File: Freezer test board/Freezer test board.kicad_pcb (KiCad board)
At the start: 4 copper layers, 56 x 65 mm, 24 parts, among them J2 Conn_02x20_Odd_Even, J3 284391-3, J4 284391-3, J5 284391-3, J6 284391-3, J7 284391-3, J8 284391-3, J9 284391-3

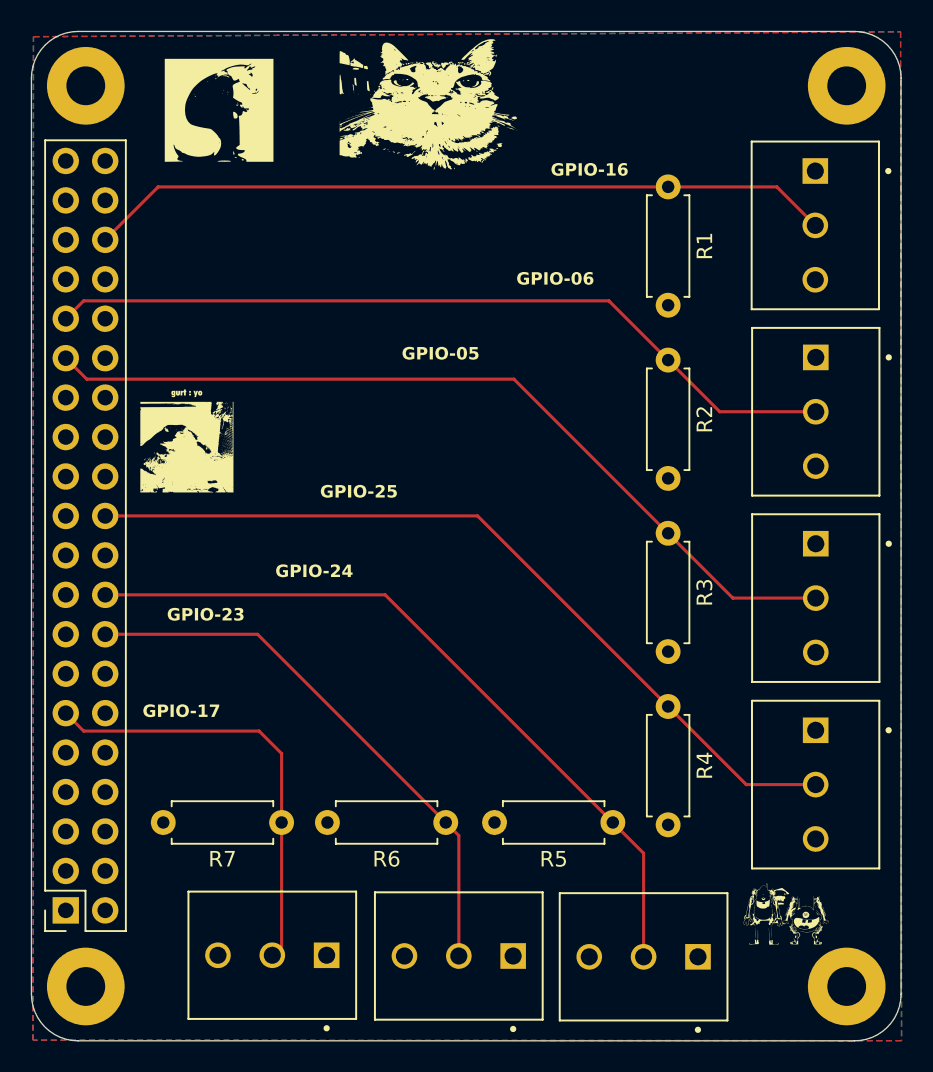
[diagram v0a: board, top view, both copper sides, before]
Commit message: Filled copper, adjust mask+silkscreens arts
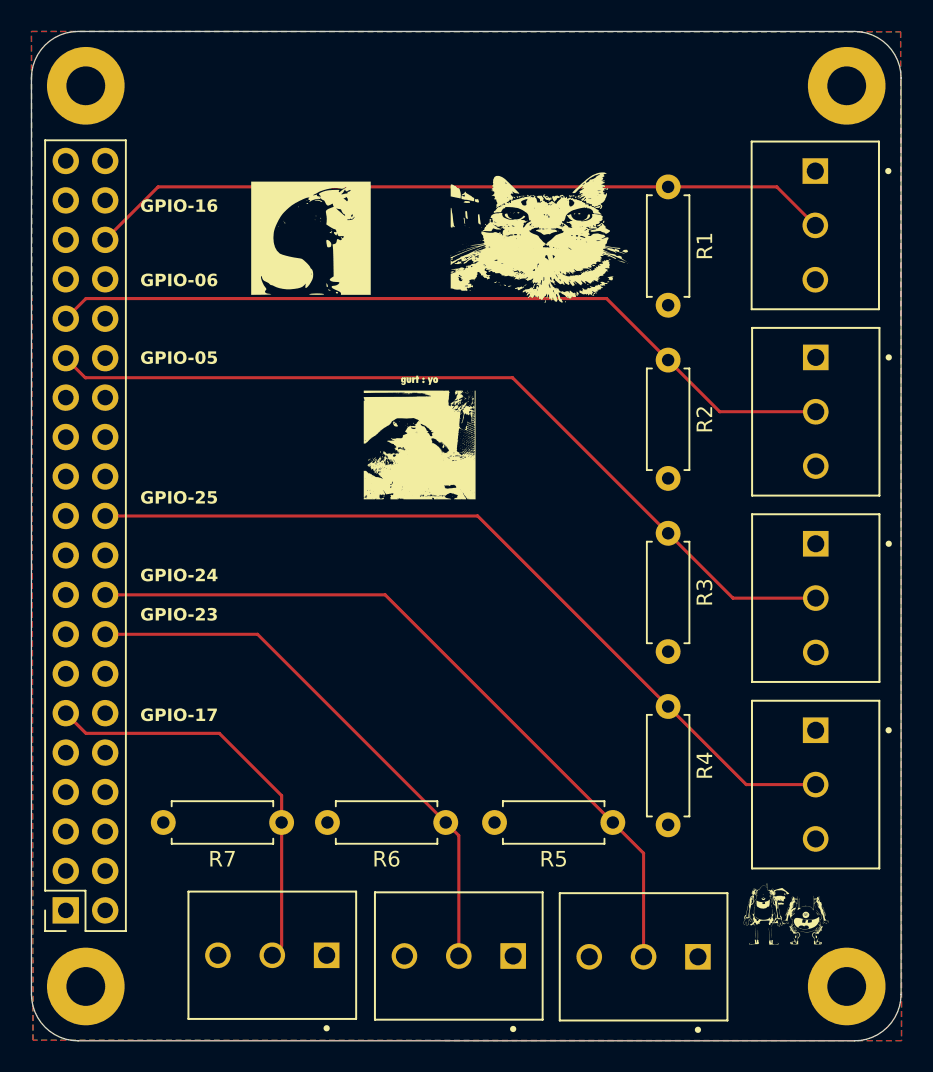
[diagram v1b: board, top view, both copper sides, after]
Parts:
- moved G*** 15.0 mm to (110.5, 63.0)
- moved G*** 11.2 mm to (118.5, 50.0)
- moved G*** 10.1 mm to (104.5, 50.0)
- moved G*** 4.01 mm to (111.5, 69.5)
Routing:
- net GPIO17: track 28.2 -> 26.6 mm
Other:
- board text added: "67 reviews later..."
- board text added: "Bronco STAR BLADE '26"
- board text added: "Designed by Jason Suarez"
- board text added: "Freezer Test Pi HAT 1.0"
- board text removed: "Freezer Test PCB"
- board text removed: "Made By Jason Suarez"

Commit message: Adjust mounting hole footprint to 2.7mm M2.5
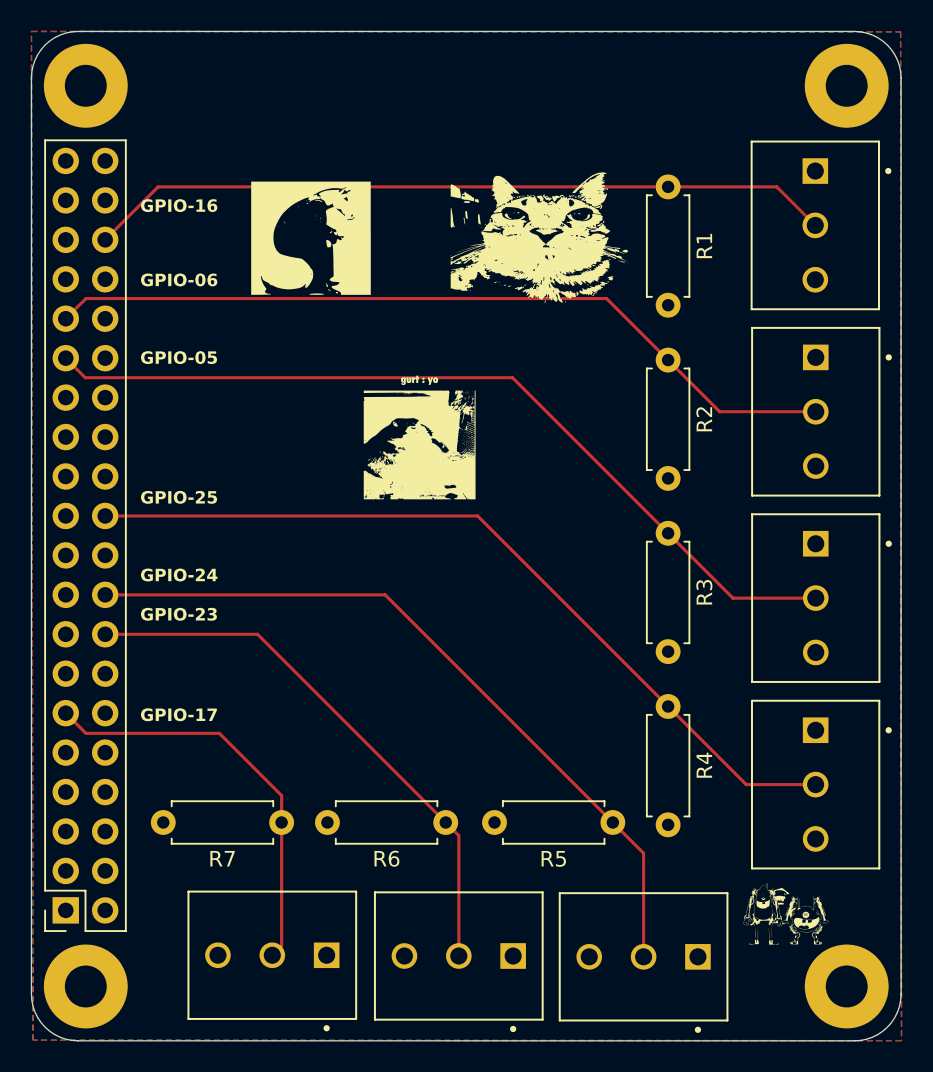
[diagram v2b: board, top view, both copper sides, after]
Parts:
- H1, H2, H3, H4: footprint MountingHole:MountingHole_2.5mm_Pad -> MountingHole:MountingHole_2.7mm_M2.5_Pad
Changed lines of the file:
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@@
 			)
 		)
-		(property "Datasheet" "~"
+		(property "Datasheet" ""
 			(at 0 0 180)
 			(layer "F.Fab")
@@
 			)
 		)
-		(property "Datasheet" "~"
+		(property "Datasheet" ""
 			(at 0 0 90)
 			(layer "F.Fab")
@@
 			)
 		)
-		(property "Datasheet" "~"
+		(property "Datasheet" ""
 			(at 0 0 0)
 			(layer "F.Fab")
@@
 			)
 		)
-		(property "Datasheet" "~"
+		(property "Datasheet" ""
 			(at 0 0 270)
 			(layer "F.Fab")
@@
 		)
 	)
-	(footprint "MountingHole:MountingHole_2.5mm_Pad"
+	(footprint "MountingHole:MountingHole_2.7mm_M2.5_Pad"
 		(layer "F.Cu")
 		(at 89 98.5)
-		(descr "Mounting Hole 2.5mm, generated by kicad-footprint-generator mountinghole.py")
-		(tags "mountinghole")
+		(descr "Mounting Hole 2.7mm, M2.5, generated by kicad-footprint-generator mountinghole.py")
+		(tags "mountinghole M2.5")
 		(property "Reference" "H2"
-			(at 4.61 0 0)
+			(at 0 -3.65 0)
 			(layer "F.SilkS")
 			(hide yes)
@@
 		)
 		(property "Value" "MountingHole"
-			(at 0 3.45 0)
+			(at 0 3.65 0)
 			(layer "F.Fab")
 			(effects
@@
 			)
 		)
-		(property "Datasheet" "~"
+		(property "Datasheet" ""
 			(at 0 0 0)
 			(layer "F.Fab")
@@
 		(sheetname "/")
 		(sheetfile "Freezer test board.kicad_sch")
-		(attr through_hole exclude_from_pos_files exclude_from_bom)
+		(attr exclude_from_pos_files exclude_from_bom)
 		(fp_circle
 			(center 0 0)
-			(end 2.5 0)
+			(end 2.7 0)
 			(stroke
 				(width 0.15)
@@
 		(fp_circle
 			(center 0 0)
-			(end 2.75 0)
+			(end 2.95 0)
 			(stroke
 				(width 0.05)
@@
 		(pad "1" thru_hole circle
 			(at 0 0)
-			(size 5 5)
-			(drill 2.5)
+			(size 5.4 5.4)
+			(drill 2.7)
 			(layers "*.Cu" "*.Mask")
 			(remove_unused_layers no)
@@
 			)
 		)
-		(property "Datasheet" "~"
+		(property "Datasheet" ""
 			(at 0 0 270)
 			(layer "F.Fab")
@@
 		)
 	)
-	(footprint "MountingHole:MountingHole_2.5mm_Pad"
+	(footprint "MountingHole:MountingHole_2.7mm_M2.5_Pad"
 		(layer "F.Cu")
 		(at 138 98.5)
-		(descr "Mounting Hole 2.5mm, generated by kicad-footprint-generator mountinghole.py")
-		(tags "mountinghole")
+		(descr "Mounting Hole 2.7mm, M2.5, generated by kicad-footprint-generator mountinghole.py")
+		(tags "mountinghole M2.5")
 		(property "Reference" "H4"
-			(at -4.23 -0.02 0)
+			(at 0 -3.65 0)
 			(layer "F.SilkS")
 			(hide yes)
@@
 		)
 		(property "Value" "MountingHole"
-			(at 0 3.45 0)
+			(at 0 3.65 0)
 			(layer "F.Fab")
 			(effects
@@
 			)
 		)
-		(property "Datasheet" "~"
+		(property "Datasheet" ""
 			(at 0 0 0)
 			(layer "F.Fab")
@@
 		(sheetname "/")
 		(sheetfile "Freezer test board.kicad_sch")
-		(attr through_hole exclude_from_pos_files exclude_from_bom)
+		(attr exclude_from_pos_files exclude_from_bom)
 		(fp_circle
 			(center 0 0)
-			(end 2.5 0)
+			(end 2.7 0)
 			(stroke
 				(width 0.15)
@@
 		(fp_circle
 			(center 0 0)
-			(end 2.75 0)
+			(end 2.95 0)
 			(stroke
 				(width 0.05)
@@
 		(pad "1" thru_hole circle
 			(at 0 0)
-			(size 5 5)
-			(drill 2.5)
+			(size 5.4 5.4)
+			(drill 2.7)
 			(layers "*.Cu" "*.Mask")
 			(remove_unused_layers no)
@@
 			)
 		)
-		(property "Datasheet" "~"
+		(property "Datasheet" ""
 			(at 0 0 270)
 			(layer "F.Fab")
@@
 			)
 		)
-		(property "Datasheet" "~"
+		(property "Datasheet" ""
 			(at 0 0 180)
 			(layer "F.Fab")
@@
 		)
 	)
-	(footprint "MountingHole:MountingHole_2.5mm_Pad"
+	(footprint "MountingHole:MountingHole_2.7mm_M2.5_Pad"
 		(layer "F.Cu")
 		(at 138 40.5)
-		(descr "Mounting Hole 2.5mm, generated by kicad-footprint-generator mountinghole.py")
-		(tags "mountinghole")
+		(descr "Mounting Hole 2.7mm, M2.5, generated by kicad-footprint-generator mountinghole.py")
+		(tags "mountinghole M2.5")
 		(property "Reference" "H3"
-			(at -4.48 0.05 0)
+			(at 0 -3.65 0)
 			(layer "F.SilkS")
 			(hide yes)
@@
 		)
 		(property "Value" "MountingHole"
-			(at 0 3.45 0)
+			(at 0 3.65 0)
 			(layer "F.Fab")
 			(effects
@@
 			)
 		)
-		(property "Datasheet" "~"
+		(property "Datasheet" ""
 			(at 0 0 0)
 			(layer "F.Fab")
@@
 		(sheetname "/")
 		(sheetfile "Freezer test board.kicad_sch")
-		(attr through_hole exclude_from_pos_files exclude_from_bom)
+		(attr exclude_from_pos_files exclude_from_bom)
 		(fp_circle
 			(center 0 0)
-			(end 2.5 0)
+			(end 2.7 0)
 			(stroke
 				(width 0.15)
@@
 		(fp_circle
 			(center 0 0)
-			(end 2.75 0)
+			(end 2.95 0)
 			(stroke
 				(width 0.05)
@@
 		(pad "1" thru_hole circle
 			(at 0 0)
-			(size 5 5)
-			(drill 2.5)
+			(size 5.4 5.4)
+			(drill 2.7)
 			(layers "*.Cu" "*.Mask")
 			(remove_unused_layers no)
@@
 			)
 		)
-		(property "Datasheet" "~"
+		(property "Datasheet" ""
 			(at 0 0 180)
 			(layer "F.Fab")
@@
 		(embedded_fonts no)
 	)
-	(footprint "MountingHole:MountingHole_2.5mm_Pad"
+	(footprint "MountingHole:MountingHole_2.7mm_M2.5_Pad"
 		(layer "F.Cu")
 		(at 89 40.5)
-		(descr "Mounting Hole 2.5mm, generated by kicad-footprint-generator mountinghole.py")
-		(tags "mountinghole")
+		(descr "Mounting Hole 2.7mm, M2.5, generated by kicad-footprint-generator mountinghole.py")
+		(tags "mountinghole M2.5")
 		(property "Reference" "H1"
-			(at 3.92 0.02 0)
+			(at 0 -3.65 0)
 			(layer "F.SilkS")
 			(hide yes)
@@
 		)
 		(property "Value" "MountingHole"
-			(at 0 3.45 0)
+			(at 0 3.65 0)
 			(layer "F.Fab")
 			(effects
@@
 			)
 		)
-		(property "Datasheet" "~"
+		(property "Datasheet" ""
 			(at 0 0 0)
 			(layer "F.Fab")
@@
 		(sheetname "/")
 		(sheetfile "Freezer test board.kicad_sch")
-		(attr through_hole exclude_from_pos_files exclude_from_bom)
+		(attr exclude_from_pos_files exclude_from_bom)
 		(fp_circle
 			(center 0 0)
-			(end 2.5 0)
+			(end 2.7 0)
 			(stroke
 				(width 0.15)
@@
 		(fp_circle
 			(center 0 0)
-			(end 2.75 0)
+			(end 2.95 0)
 			(stroke
 				(width 0.05)
@@
 		(pad "1" thru_hole circle
 			(at 0 0)
-			(size 5 5)
-			(drill 2.5)
+			(size 5.4 5.4)
+			(drill 2.7)
 			(layers "*.Cu" "*.Mask")
 			(remove_unused_layers no)
